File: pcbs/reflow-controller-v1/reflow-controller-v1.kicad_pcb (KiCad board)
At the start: 4 copper layers, 85.2 x 238.5 mm, 137 parts, among them J1 PinHeader 1x03 P2.54mm, J101 EB163A-03-C-180, J102 EB163A-02-C-180, J103 EB163A-02-C-180, J104 EB163A-02-C-180, J105 EB163A-02-C-180, J106 PinHeader 1x03 P2.54mm, J1101 EB163A-04-C-180, J1201 EB163A-04-C-180, J1301 EB163A-04-C-180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

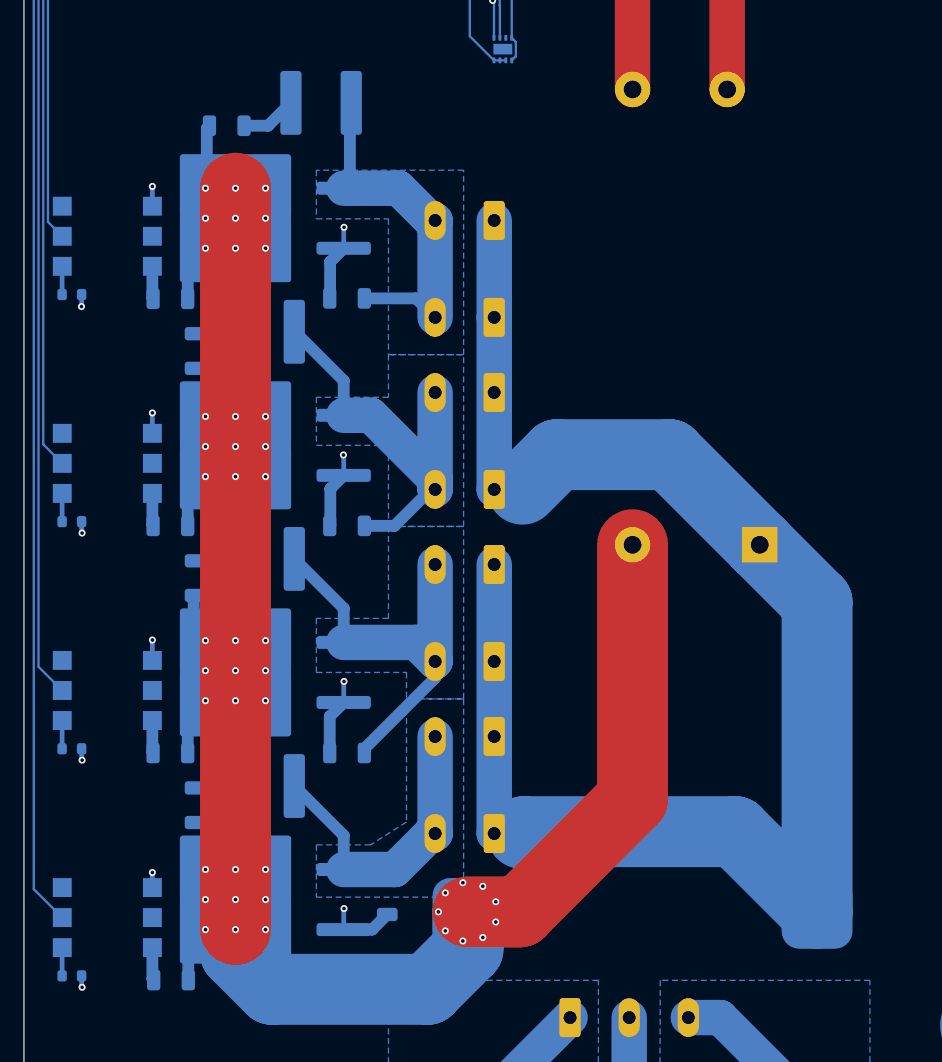
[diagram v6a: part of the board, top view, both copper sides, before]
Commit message: implement first layout feedback
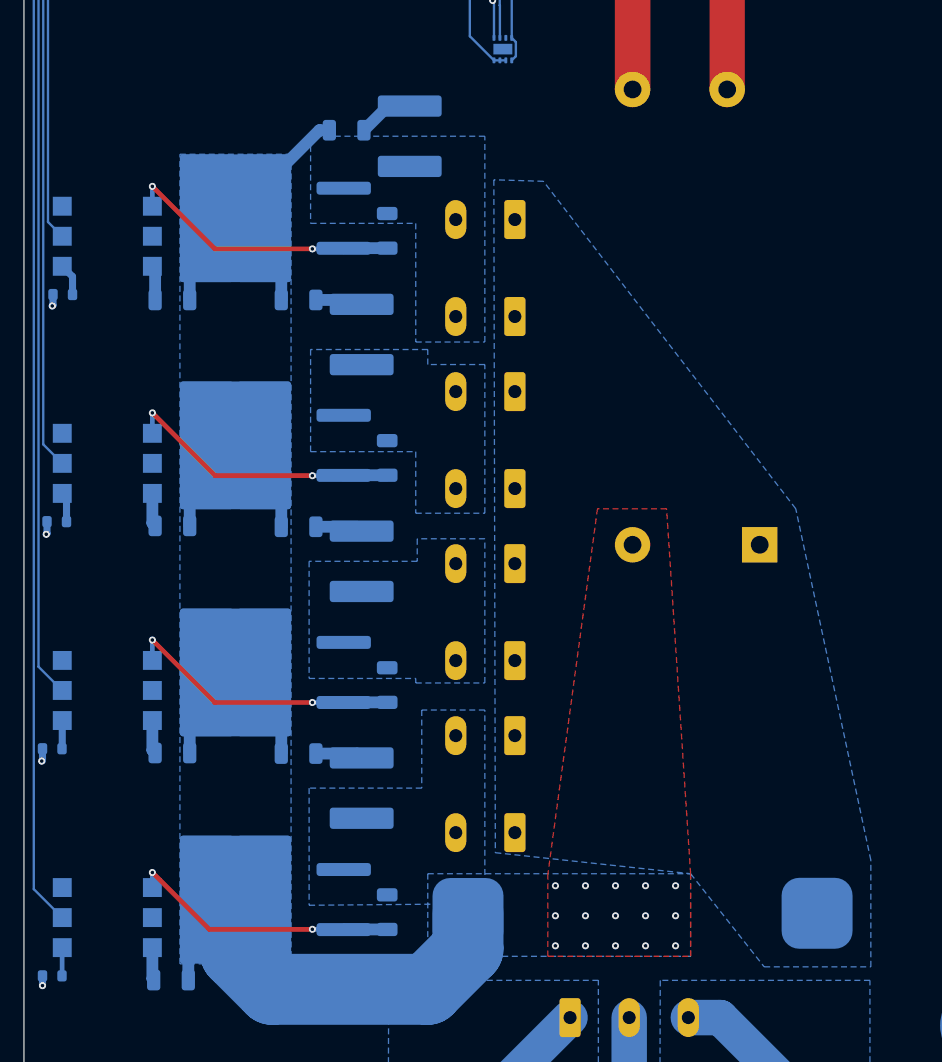
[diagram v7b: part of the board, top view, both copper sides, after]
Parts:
- moved R305 10.1 mm to (43.7, 160.5)
- moved R604 9.78 mm to (39.6, 213.2), turned to 0 degrees
- moved R504 9.77 mm to (39.6, 194.1), turned to 0 degrees
- moved R404 9.76 mm to (39.6, 174.9), turned to 0 degrees
- moved C401 8.25 mm to (45.0, 177.8), turned to -90 degrees
- moved C501 8.25 mm to (45.0, 197.0), turned to -90 degrees
- moved C601 8.25 mm to (45.0, 216.2), turned to -90 degrees
- moved C301 8.01 mm to (49.0, 161.0), turned to -90 degrees
- moved R402 6.67 mm to (47.1, 188.2), turned to 90 degrees
- moved R502 6.67 mm to (47.1, 207.4), turned to 90 degrees
- moved R304 6.64 mm to (47.1, 169.0), turned to 90 degrees
- moved J102 1.75 mm to (57.9, 168.1)
- moved J103 1.75 mm to (57.9, 182.6)
- moved J104 1.75 mm to (57.9, 197.2)
- moved J105 1.75 mm to (57.9, 211.7)
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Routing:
- net /Phase_N: track 135.7 -> 0.00 mm
- net /Phase_L: track 162.5 -> 72.5 mm, vias 45 -> 15
- net /SSR 3/MAIN_OUT: track 35.6 -> 0.00 mm
- net /SSR 2/MAIN_OUT: track 35.1 -> 0.00 mm
- net /SSR 1/MAIN_OUT: track 31.2 -> 0.00 mm
- net /SSR 4/MAIN_OUT: track 26.0 -> 0.00 mm
- net Net-(D501-G): track 28.3 -> 23.8 mm
- net Net-(D301-G): track 27.4 -> 23.7 mm
- net Net-(D601-G): track 26.6 -> 23.1 mm
- net Net-(D401-G): track 27.3 -> 23.8 mm
- net Net-(C601-Pad1): track 3.36 -> 4.03 mm
- net Net-(C401-Pad1): track 3.36 -> 4.03 mm
- net Net-(C501-Pad1): track 3.36 -> 4.03 mm
- added copper zone on B.Cu, net /Phase_L
- added copper zone on F.Cu, net /Phase_L
- added copper zone on B.Cu, net /Phase_N
